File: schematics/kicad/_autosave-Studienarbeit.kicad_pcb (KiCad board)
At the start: 2 copper layers, 67 parts, among them U1 ESP32-WROOM-32E, U2 PCM5102, U3 MCP6001-OT, U4 MCP6001-OT, U5 MCP6001, U6 TPA711, U7 LM2940CT-5.0

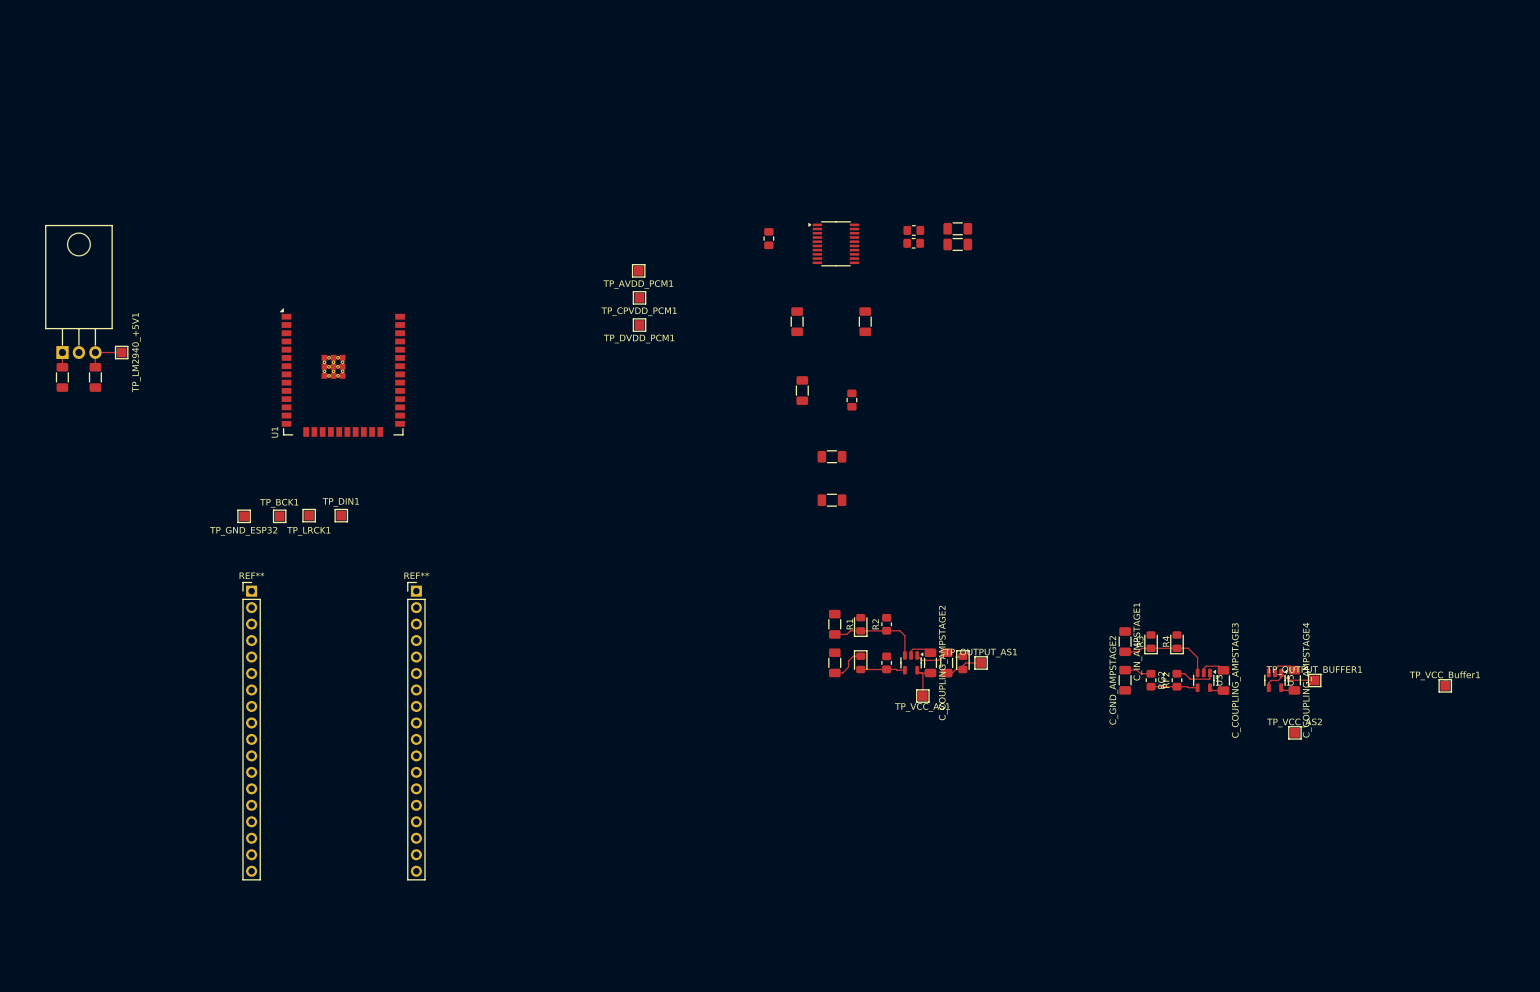
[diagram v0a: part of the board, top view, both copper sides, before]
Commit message: Replace ESP32 Schematic with header pins.
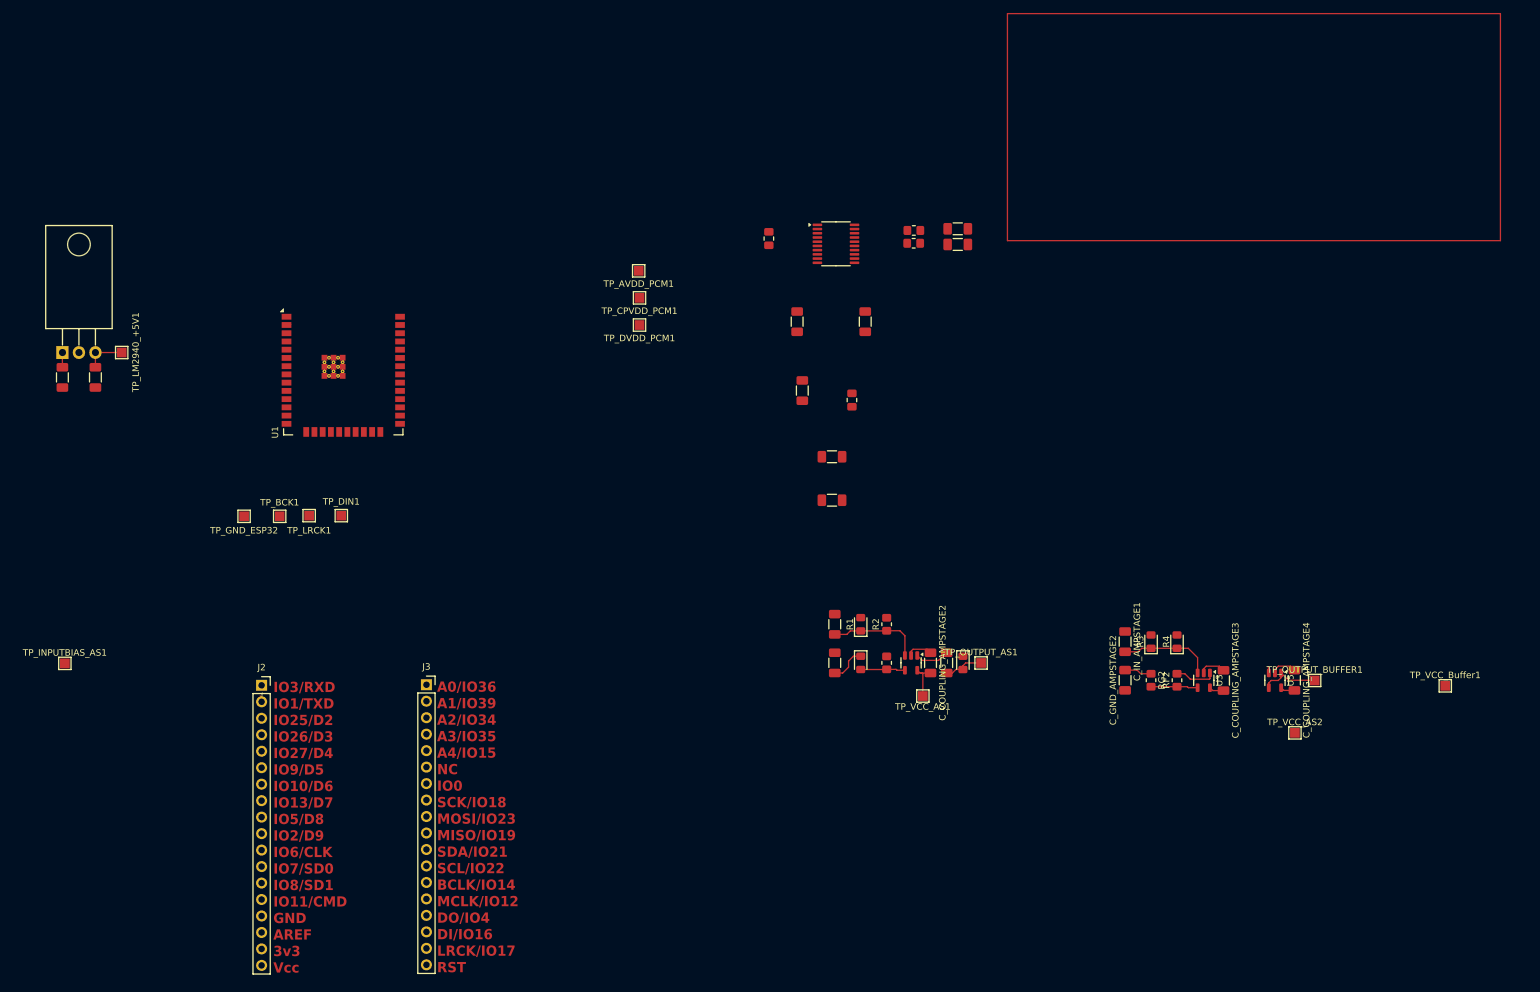
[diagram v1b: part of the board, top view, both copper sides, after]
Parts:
- removed REF** (x2): PinHeader_1x18_P2.54mm_Vertical, Connector_PinHeader_2.54mm:PinHeader_1x18_P2.54mm_Vertical
- added J2: Conn_01x18, Connector_PinSocket_2.54mm:PinSocket_1x18_P2.54mm_Vertical, F.Cu at (63.7, 137.1)
- added J3: Conn_01x18, Connector_PinSocket_2.54mm:PinSocket_1x18_P2.54mm_Vertical, F.Cu at (89.1, 137.0)
- added TP_INPUTBIAS_AS1: TestPoint, TestPoint:TestPoint_Pad_1.5x1.5mm, F.Cu at (33.3, 133.7)
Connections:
- net /LRCK renamed /IO12
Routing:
- net unconnected-(J2-Pin_2-Pad2): track 0.00 -> 0.90 mm
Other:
- board text added: "A0/IO36 A1/IO39 A2/IO34 A3/IO35 A4/IO15 NC IO0 SCK/IO18 MOSI/IO23 MISO/IO19 SDA/IO21 SCL/IO22 BCLK/IO14 MCLK/IO12 DO/IO4 DI/IO16 LRCK/IO17 RST"
- board text added: "IO3/RXD IO1/TXD IO25/D2 IO26/D3 IO27/D4 IO9/D5 IO10/D6 IO13/D7 IO5/D8 IO2/D9 IO6/CLK IO7/SD0 IO8/SD1 IO11/CMD GND AREF 3v3 Vcc"
